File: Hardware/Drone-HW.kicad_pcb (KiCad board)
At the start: 2 copper layers, 61.5 x 40 mm, 26 parts, among them Con5 espTool_conn, J5 Conn_01x02_Pin, M1 Conn_01x01_Pin, M2 Conn_01x01_Pin, M3 Conn_01x01_Pin, M4 Conn_01x01_Pin, Q5 BC846, Q6 BC846, SW3 Tactile, U1 ESP32-WROOM-32D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

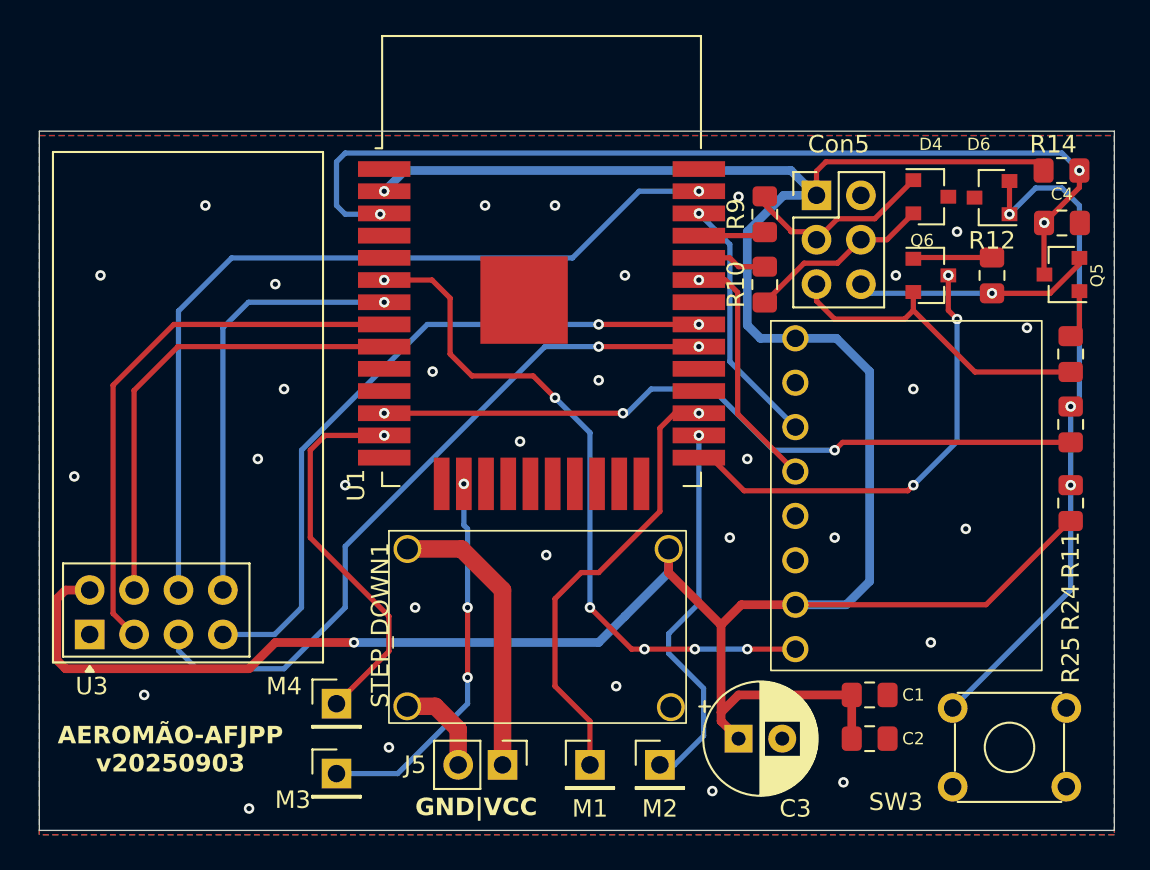
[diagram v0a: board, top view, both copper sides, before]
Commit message: Retirando modulos escs da pcb
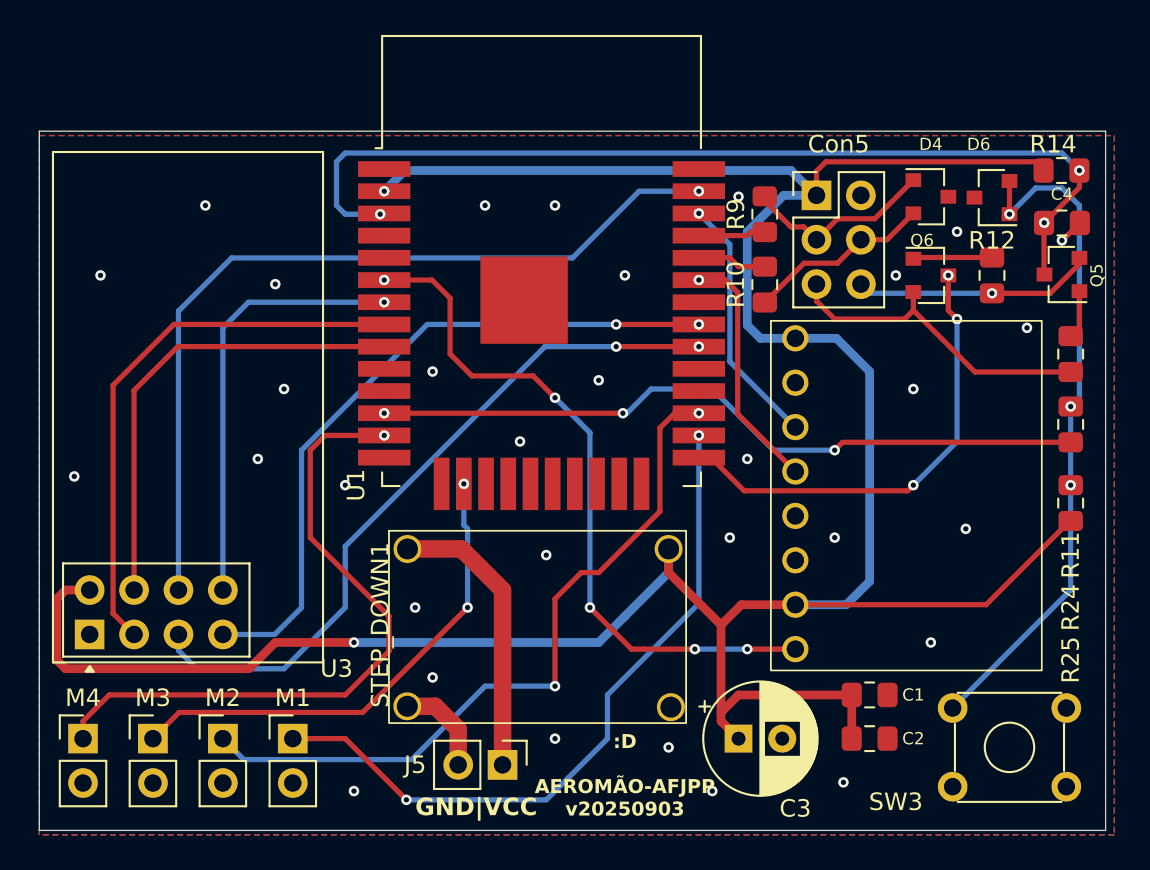
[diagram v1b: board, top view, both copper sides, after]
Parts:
- M1, M2, M3, M4: value Conn_01x01_Pin -> pinH_2v; footprint Connector_PinHeader_2.54mm:PinHeader_1x01_P2.54mm_Vertical -> Local_Connector_PinHeader_2.54mm:PinHeader_1x02_P2.54mm_Vertical
- moved M2 25.0 mm to (144.5, 68.5)
- moved M1 17.1 mm to (148.5, 68.5)
- moved M4 14.6 mm to (136.5, 68.5)
- moved M3 10.7 mm to (140.5, 68.5)
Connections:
- U1 pad 26: /Motor2 -> /Motor1
- U1 pad 27: /Motor1 -> /Motor2
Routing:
- net /Motor2: track 21.9 -> 41.7 mm, vias 1 -> 2
- net /Motor4: track 22.2 -> 38.1 mm
- net /Motor1: track 25.7 -> 40.4 mm, vias 1 -> 2
- net /Motor3: track 21.8 -> 28.3 mm, vias 3 -> 2
- net GND: track 0.00 -> 1.44 mm, vias 31 -> 32
- net /INT: vias 6 -> 5
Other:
- board size 61.5 x 40 mm -> 61 x 40 mm
- board text added: ":D AEROMÃO-AFJPP v20250903"
- board text removed: "AEROMÃO-AFJPP v20250903"
